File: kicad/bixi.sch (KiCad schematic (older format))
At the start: 37 parts, among them J1 RJ45, J2 RJ45, J3 RJ45, J4 RJ45, J5 RJ45, J6 RJ45, J7 RJ45, J8 RJ45, U1 SP3481CN, U10 ESP8266, U2 SP3481CN, U3 SP3481CN, U4 SP3481CN, U5 SP3481CN, U6 SP3481CN, U7 SP3481CN, U8 SP3481CN, U9 Teensy3.6

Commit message: fixes to boards, node still in progress
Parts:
- C1, C2, C3, C4, C5, C6, C7, C8, C9: footprint Capacitors_THT:C_Disc_D4.7mm_W2.5mm_P5.00mm -> Capacitors_THT:C_Axial_L3.8mm_D2.6mm_P7.50mm_Horizontal
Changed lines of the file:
@@
 F 0 "C9" H 5925 1100 50  0000 L CNN
 F 1 "C" H 5925 900 50  0000 L CNN
-F 2 "Capacitors_THT:C_Disc_D4.7mm_W2.5mm_P5.00mm" H 5938 850 50  0001 C CNN
+F 2 "Capacitors_THT:C_Axial_L3.8mm_D2.6mm_P7.50mm_Horizontal" H 5938 850 50  0001 C CNN
 F 3 "" H 5900 1000 50  0001 C CNN
 	1    5900 1000
@@
 F 0 "C1" H 4875 5050 50  0000 L CNN
 F 1 "C" H 4875 4850 50  0000 L CNN
-F 2 "Capacitors_THT:C_Disc_D4.7mm_W2.5mm_P5.00mm" H 4888 4800 50  0001 C CNN
+F 2 "Capacitors_THT:C_Axial_L3.8mm_D2.6mm_P7.50mm_Horizontal" H 4888 4800 50  0001 C CNN
 F 3 "" H 4850 4950 50  0001 C CNN
 	1    4850 4950
@@
 F 0 "C2" H 5125 5050 50  0000 L CNN
 F 1 "C" H 5125 4850 50  0000 L CNN
-F 2 "Capacitors_THT:C_Disc_D4.7mm_W2.5mm_P5.00mm" H 5138 4800 50  0001 C CNN
+F 2 "Capacitors_THT:C_Axial_L3.8mm_D2.6mm_P7.50mm_Horizontal" H 5138 4800 50  0001 C CNN
 F 3 "" H 5100 4950 50  0001 C CNN
 	1    5100 4950
@@
 F 0 "C3" H 5375 5050 50  0000 L CNN
 F 1 "C" H 5375 4850 50  0000 L CNN
-F 2 "Capacitors_THT:C_Disc_D4.7mm_W2.5mm_P5.00mm" H 5388 4800 50  0001 C CNN
+F 2 "Capacitors_THT:C_Axial_L3.8mm_D2.6mm_P7.50mm_Horizontal" H 5388 4800 50  0001 C CNN
 F 3 "" H 5350 4950 50  0001 C CNN
 	1    5350 4950
@@
 F 0 "C4" H 5625 5050 50  0000 L CNN
 F 1 "C" H 5625 4850 50  0000 L CNN
-F 2 "Capacitors_THT:C_Disc_D4.7mm_W2.5mm_P5.00mm" H 5638 4800 50  0001 C CNN
+F 2 "Capacitors_THT:C_Axial_L3.8mm_D2.6mm_P7.50mm_Horizontal" H 5638 4800 50  0001 C CNN
 F 3 "" H 5600 4950 50  0001 C CNN
 	1    5600 4950
@@
 F 0 "C5" H 5875 5050 50  0000 L CNN
 F 1 "C" H 5875 4850 50  0000 L CNN
-F 2 "Capacitors_THT:C_Disc_D4.7mm_W2.5mm_P5.00mm" H 5888 4800 50  0001 C CNN
+F 2 "Capacitors_THT:C_Axial_L3.8mm_D2.6mm_P7.50mm_Horizontal" H 5888 4800 50  0001 C CNN
 F 3 "" H 5850 4950 50  0001 C CNN
 	1    5850 4950
@@
 F 0 "C6" H 6125 5050 50  0000 L CNN
 F 1 "C" H 6125 4850 50  0000 L CNN
-F 2 "Capacitors_THT:C_Disc_D4.7mm_W2.5mm_P5.00mm" H 6138 4800 50  0001 C CNN
+F 2 "Capacitors_THT:C_Axial_L3.8mm_D2.6mm_P7.50mm_Horizontal" H 6138 4800 50  0001 C CNN
 F 3 "" H 6100 4950 50  0001 C CNN
 	1    6100 4950
@@
 F 0 "C7" H 6375 5050 50  0000 L CNN
 F 1 "C" H 6375 4850 50  0000 L CNN
-F 2 "Capacitors_THT:C_Disc_D4.7mm_W2.5mm_P5.00mm" H 6388 4800 50  0001 C CNN
+F 2 "Capacitors_THT:C_Axial_L3.8mm_D2.6mm_P7.50mm_Horizontal" H 6388 4800 50  0001 C CNN
 F 3 "" H 6350 4950 50  0001 C CNN
 	1    6350 4950
@@
 F 0 "C8" H 6625 5050 50  0000 L CNN
 F 1 "C" H 6625 4850 50  0000 L CNN
-F 2 "Capacitors_THT:C_Disc_D4.7mm_W2.5mm_P5.00mm" H 6638 4800 50  0001 C CNN
+F 2 "Capacitors_THT:C_Axial_L3.8mm_D2.6mm_P7.50mm_Horizontal" H 6638 4800 50  0001 C CNN
 F 3 "" H 6600 4950 50  0001 C CNN
 	1    6600 4950

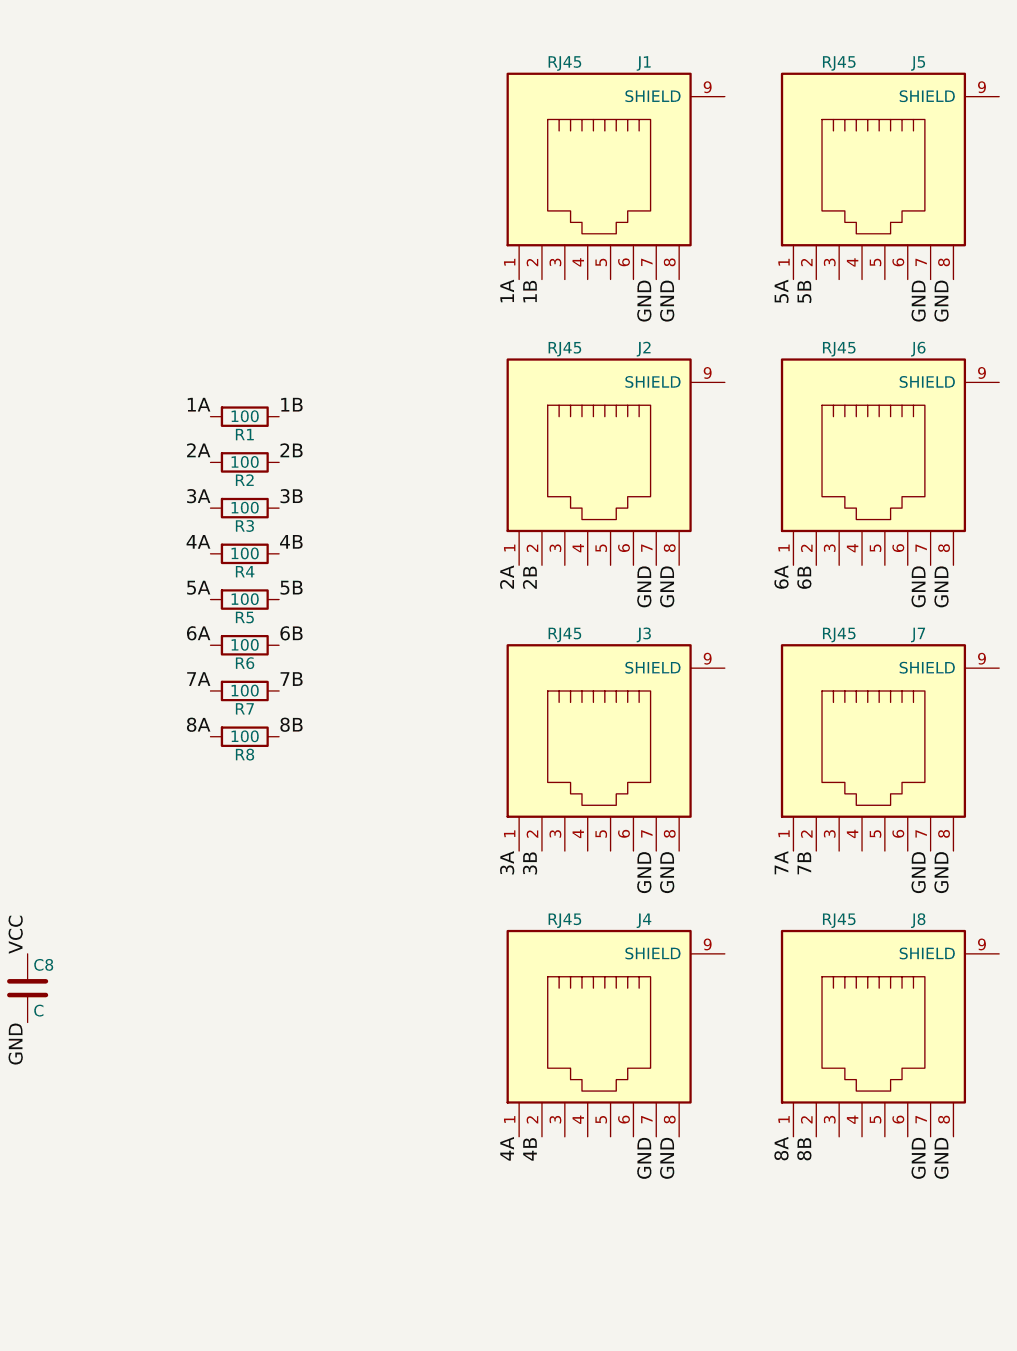
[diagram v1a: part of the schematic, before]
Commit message: updated controller board with stacked rj45
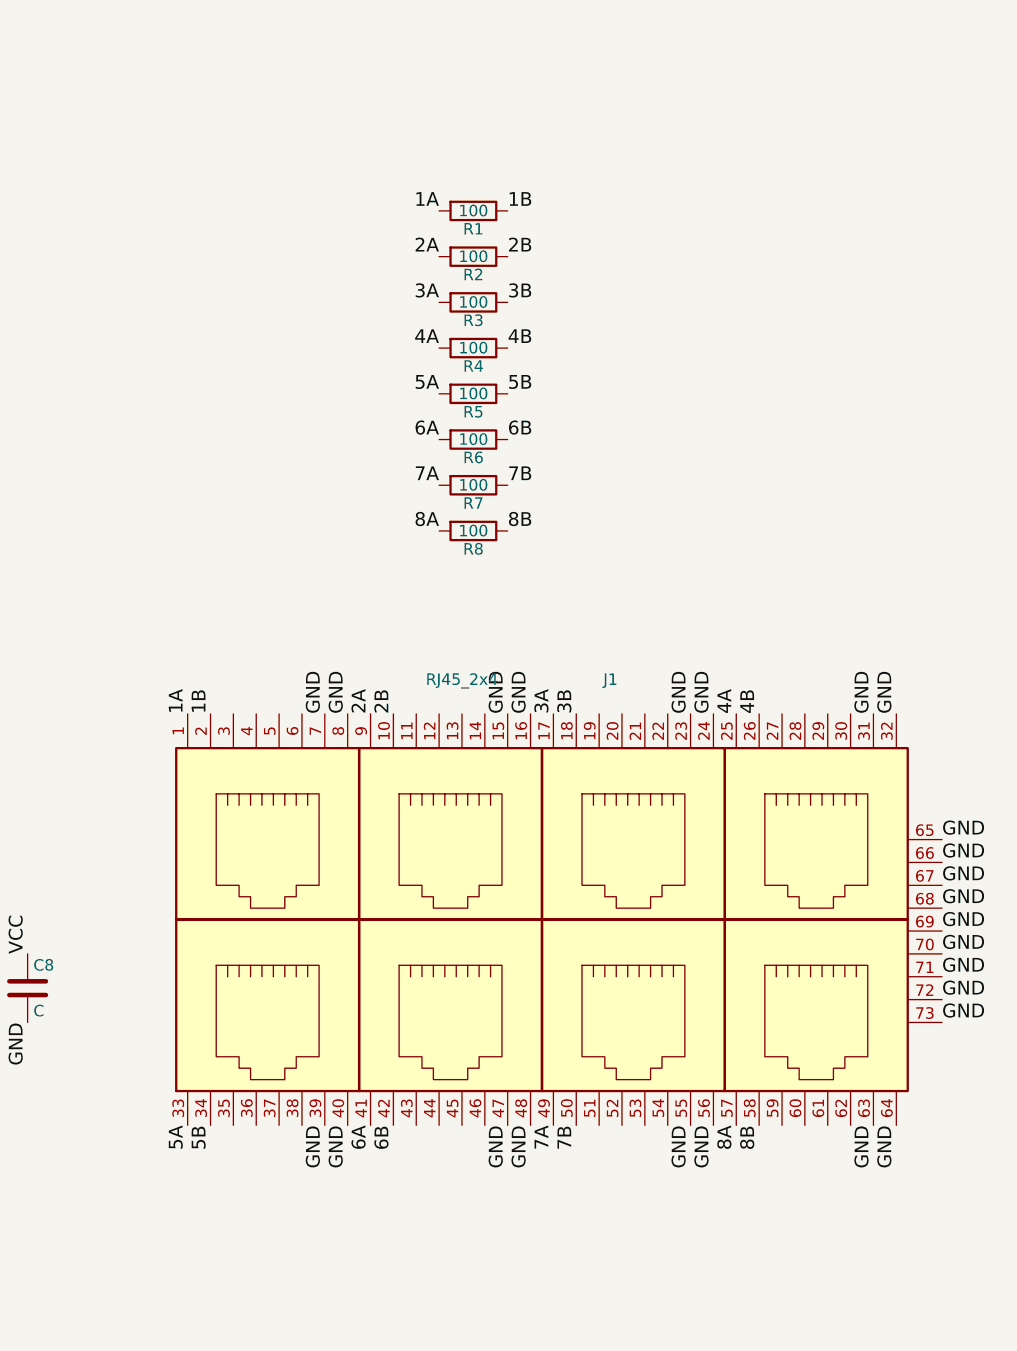
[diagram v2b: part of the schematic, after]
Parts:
- removed J1, J2, J3, J4, J5, J6, J7, J8: RJ45, Connectors:RJ45_8, symbol RJ45
- added J1: RJ45_2x4, custom:RJ45_2x4, symbol RJ45_2x4
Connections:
- net 1A: now also J1.1
- net 1B: now also J1.2
- net 2A: now also J1.9
- net 2B: now also J1.10
- net 3A: now also J1.17
- net 3B: now also J1.18
- net 4A: now also J1.25
- net 4B: now also J1.26
- net 5A: now also J1.33
- net 5B: now also J1.34
- net 6A: now also J1.41
- net 6B: now also J1.42
- net 7A: now also J1.49
- net 7B: now also J1.50
- net 8A: now also J1.57
- net 8B: now also J1.58
- net GND: now also J1.15, J1.16, J1.23, J1.24, J1.31, J1.32, J1.39, J1.40, J1.47, J1.48, J1.55, J1.56, J1.63, J1.64, J1.65, J1.66, J1.67, J1.68, J1.69, J1.7, J1.70, J1.71, J1.72, J1.73, J1.8
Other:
- moved on the sheet: R1, R2, R3, R4, R5, R6, R7, R8
